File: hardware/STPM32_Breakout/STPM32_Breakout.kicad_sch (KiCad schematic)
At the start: 0 parts

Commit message: Complete compact STPM32 breakout
Implement the isolated 9 VAC and current-output CT front end, compact breadboard PCB, routed ground planes, validation scripts, and design documentation.

Co-authored-by: Copilot <223556219+Copilot@users.noreply.github.com>
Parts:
- added C1, C2: 330n, Capacitor_SMD:C_0603_1608Metric, symbol Device:C
- added C10, C9: 1u, Capacitor_SMD:C_0805_2012Metric, symbol Device:C
- added C11: 4.7u, Capacitor_SMD:C_0805_2012Metric, symbol Device:C
- added C12: 100n, Capacitor_SMD:C_0603_1608Metric, symbol Device:C
- added C13, C14: 15p, Capacitor_SMD:C_0603_1608Metric, symbol Device:C
- added C3, C4: 33n, Capacitor_SMD:C_0603_1608Metric, symbol Device:C
- added J1: BREADBOARD I/O, Connector_PinHeader_2.54mm:PinHeader_1x12_P2.54mm_Vertical, symbol Connector_Generic:Conn_01x12
- added NT1: ANALOG/DIGITAL STAR, NetTie:NetTie-3_SMD_Pad0.5mm, symbol Connector_Generic:Conn_01x03
- added R1, R2: 100R, Resistor_SMD:R_0603_1608Metric, symbol Device:R
- added R10, R9: 1k, Resistor_SMD:R_0603_1608Metric, symbol Device:R
- added R11, R12: 10k, Resistor_SMD:R_0603_1608Metric, symbol Device:R
- added R3, R4, R6, R7: 100k, Resistor_SMD:R_0603_1608Metric, symbol Device:R
- added R5, R8: 2.49k, Resistor_SMD:R_0603_1608Metric, symbol Device:R
- added RB1: 2.4R, Resistor_SMD:R_0603_1608Metric, symbol Device:R
- added SW1: RESET, Button_Switch_SMD:SW_SPST_CK_RS282G05A3, symbol Switch:SW_Push
- added TP1: INT1, TestPoint:TestPoint_Pad_D1.5mm, symbol Connector_Generic:Conn_01x01
- added TP2: LED1, TestPoint:TestPoint_Pad_D1.5mm, symbol Connector_Generic:Conn_01x01
- added TP3: LED2, TestPoint:TestPoint_Pad_D1.5mm, symbol Connector_Generic:Conn_01x01
- added TP4: CLKOUT_ZCR, TestPoint:TestPoint_Pad_D1.5mm, symbol Connector_Generic:Conn_01x01
- added U1: STPM32, Package_DFN_QFN:VQFN-24-1EP_4x4mm_P0.5mm_EP2.45x2.45mm, symbol STPM3x:STPM32
- added Y1: 16MHz, Crystal:Crystal_SMD_3225-4Pin_3.2x2.5mm, symbol Device:Crystal
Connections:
- new net +3V3: C9.1, J1.1 (Pin_1), R11.1, U1.17 (VCC)
- new net AGND: C1.2, C10.2, C2.2, C3.2, C4.2, NT1.1 (Pin_1), R5.2, R8.2, U1.14 (GNDA), U1.16 (GND_REG)
- new net CLKOUT_ZCR: TP4.1 (Pin_1), U1.1 (CLKOUT/ZCR)
- new net CT_N: J1.6 (Pin_6), R2.1, RB1.2
- new net CT_P: J1.5 (Pin_5), R1.1, RB1.1
- new net DGND: C11.2, C13.2, C14.2, C9.2, J1.2 (Pin_2), NT1.3 (Pin_3), R12.2, SW1.2, U1.18 (GNDD)
- new net EN: J1.12 (Pin_12), R11.2, SW1.1, U1.7 (EN)
- new net GND_REF: C12.2, NT1.2 (Pin_2), U1.13 (GND_REF)
- new net IIN1: C2.1, R2.2, U1.11 (IIN1)
- new net IIP1: C1.1, R1.2, U1.10 (IIP1)
- new net INT1: TP1.1 (Pin_1), U1.6 (INT1)
- new net LED1: TP2.1 (Pin_1), U1.4 (LED1)
- new net LED2: TP3.1 (Pin_1), U1.5 (LED2)
- new net MISO_TXD: J1.10 (Pin_10), U1.24 (MISO/TXD)
- new net MOSI_RXD: J1.9 (Pin_9), U1.23 (MOSI/RXD)
- new net SCL: J1.8 (Pin_8), U1.22 (SCL)
- new net SCS: J1.7 (Pin_7), R12.1, U1.21 (SCS)
- new net SYN: J1.11 (Pin_11), U1.20 (SYN)
- new net VAC_N: J1.4 (Pin_4), R6.1
- new net VAC_N_MID: R6.2, R7.1
- new net VAC_P: J1.3 (Pin_3), R3.1
- new net VAC_P_MID: R3.2, R4.1
- new net VDDA: C10.1, U1.15 (VDDA)
- new net VDDD: C11.1, U1.19 (VDDD)
- new net VDIV_N: R10.1, R7.2, R8.1
- new net VDIV_P: R4.2, R5.1, R9.1
- new net VIN1: C4.1, R10.2, U1.9 (VIN1)
- new net VIP1: C3.1, R9.2, U1.8 (VIP1)
- new net VREF1: C12.1, U1.12 (VREF1)
- new net XTAL1: C13.1, U1.3 (XTAL1), Y1.1
- new net XTAL2: C14.1, U1.2 (CLKIN/XTAL2), Y1.2
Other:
- note added: "CURRENT HEADER INPUT: 100 A : 50 mA current-output CT 2.4 ohm burden = 120 mV RMS at 100 A; approximately 4.8 kHz LPF."
- note added: "SCS is pulled low for SPI default; drive high before reset to select UART."
- note added: "VOLTAGE HEADER INPUT: isolated 9 VAC transformer secondary only 200k/2.49k symmetric divider = approx. 111 mV RMS differential at 9 VAC."
- note added: "WARNING: NOT A CERTIFIED ISOLATION BARRIER. Never connect J1 directly to mains."
- title: STPM32 Breakout -> STPM32 Energy Metering Breakout

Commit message: Add Elecrow BOM for STPM32
Co-authored-by: Copilot <223556219+Copilot@users.noreply.github.com>
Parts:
- C1, C2: Assembly (none) -> SMT; LCSC (none) -> C282682; MPN (none) -> TCC0603X7R334K500CT; Manufacturer (none) -> CCTC; Package (none) -> 0603 (1608 Metric); Purchase URL (none) -> https://www.lcsc.com/product-detail/C282682.html
- C10, C9: Assembly (none) -> SMT; LCSC (none) -> C116352; MPN (none) -> CL21B105KAFNNNE; Manufacturer (none) -> Samsung Electro-Mechanics; Package (none) -> 0805 (2012 Metric); Purchase URL (none) -> https://www.lcsc.com/product-detail/C116352.html
- C11: Assembly (none) -> SMT; LCSC (none) -> C16194928; MPN (none) -> CL21A475KOFNNNG; Manufacturer (none) -> Samsung Electro-Mechanics; Package (none) -> 0805 (2012 Metric); Purchase URL (none) -> https://www.lcsc.com/product-detail/C16194928.html
- C12: Assembly (none) -> SMT; LCSC (none) -> C1591; MPN (none) -> CL10B104KB8NNNC; Manufacturer (none) -> Samsung Electro-Mechanics; Package (none) -> 0603 (1608 Metric); Purchase URL (none) -> https://www.lcsc.com/product-detail/C1591.html
- C13, C14: Assembly (none) -> SMT; LCSC (none) -> C1644; MPN (none) -> CL10C150JB8NNNC; Manufacturer (none) -> Samsung Electro-Mechanics; Package (none) -> 0603 (1608 Metric); Purchase URL (none) -> https://www.lcsc.com/product-detail/C1644.html
- C3, C4: Assembly (none) -> SMT; LCSC (none) -> C21117; MPN (none) -> CL10B333KB8NNNC; Manufacturer (none) -> Samsung Electro-Mechanics; Package (none) -> 0603 (1608 Metric); Purchase URL (none) -> https://www.lcsc.com/product-detail/C21117.html
- J1: Assembly (none) -> THT; LCSC (none) -> C2840012; MPN (none) -> PZ254V-11-12P; Manufacturer (none) -> XFCN; Notes (none) -> Quote THT assembly separately and confirm pin protrusion su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; Package (none) -> 1x12, 2.54 mm pitch, vertical THT; Purchase URL (none) -> https://www.lcsc.com/product-detail/C2840012.html
- NT1, TP1, TP2, TP3, TP4: now left out of the parts list
- R1, R2: Assembly (none) -> SMT; LCSC (none) -> C105588; MPN (none) -> RC0603FR-07100RL; Manufacturer (none) -> YAGEO; Package (none) -> 0603 (1608 Metric); Purchase URL (none) -> https://www.lcsc.com/product-detail/C105588.html
- R10, R9: Assembly (none) -> SMT; LCSC (none) -> C22548; MPN (none) -> RC0603FR-071KL; Manufacturer (none) -> YAGEO; Package (none) -> 0603 (1608 Metric); Purchase URL (none) -> https://www.lcsc.com/product-detail/C22548.html
- R11, R12: Assembly (none) -> SMT; LCSC (none) -> C98220; MPN (none) -> RC0603FR-0710KL; Manufacturer (none) -> YAGEO; Package (none) -> 0603 (1608 Metric); Purchase URL (none) -> https://www.lcsc.com/product-detail/C98220.html
- R3, R4, R6, R7: Assembly (none) -> SMT; LCSC (none) -> C122538; MPN (none) -> RT0603BRD07100KL; Manufacturer (none) -> YAGEO; Notes (none) -> Use one lot for all four voltage-divider resistors.; Package (none) -> 0603 (1608 Metric); Purchase URL (none) -> https://www.lcsc.com/product-detail/C122538.html
- R5, R8: Assembly (none) -> SMT; LCSC (none) -> C861299; MPN (none) -> RT0603BRD072K49L; Manufacturer (none) -> YAGEO; Notes (none) -> Use one lot for the matched voltage-divider low sides.; Package (none) -> 0603 (1608 Metric); Purchase URL (none) -> https://www.lcsc.com/product-detail/C861299.html
- RB1: Assembly (none) -> SMT; LCSC (none) -> C137746; MPN (none) -> RC0603FR-072R4L; Manufacturer (none) -> YAGEO; Notes (none) -> About 6 mW at 50 mA RMS. The 200 ppm/C TCR is suitable for 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; Package (none) -> 0603 (1608 Metric); Purchase URL (none) -> https://www.lcsc.com/product-detail/C137746.html
- SW1: Assembly (none) -> SMT; LCSC (none) -> C221930; MPN (none) -> RS-282G05A3-SMRT; Manufacturer (none) -> C&K; Package (none) -> C&K RS-282G05A3 SMD; Purchase URL (none) -> https://www.lcsc.com/product-detail/C221930.html
- U1: Assembly (none) -> SMT; LCSC (none) -> C128380; MPN (none) -> STPM32TR; Manufacturer (none) -> STMicroelectronics; Notes (none) -> Inspect exposed-pad paste and voiding during DFM review.; Package (none) -> VQFN-24-EP, 4 x 4 mm, 0.5 mm pitch; Purchase URL (none) -> https://www.lcsc.com/product-detail/C128380.html
- Y1: Assembly (none) -> SMT; LCSC (none) -> C12668; MPN (none) -> X322516MOB4SI; Manufacturer (none) -> YXC; Notes (none) -> 12 pF load is consistent with two 15 pF capacitors plus est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; Package (none) -> SMD3225-4P; Purchase URL (none) -> https://www.lcsc.com/product-detail/C12668.html

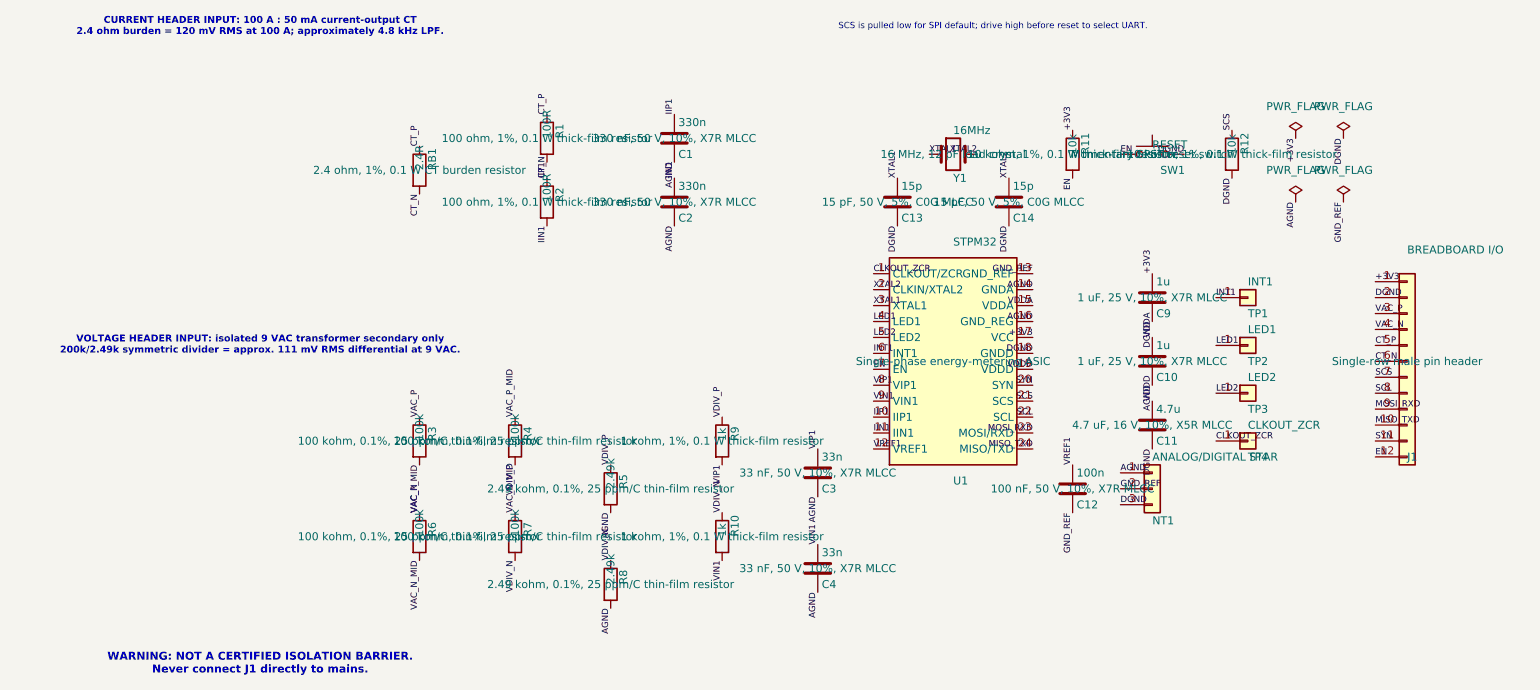
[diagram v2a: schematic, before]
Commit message: Add STPM32 SPI UART mode selector
Co-authored-by: Copilot <223556219+Copilot@users.noreply.github.com>
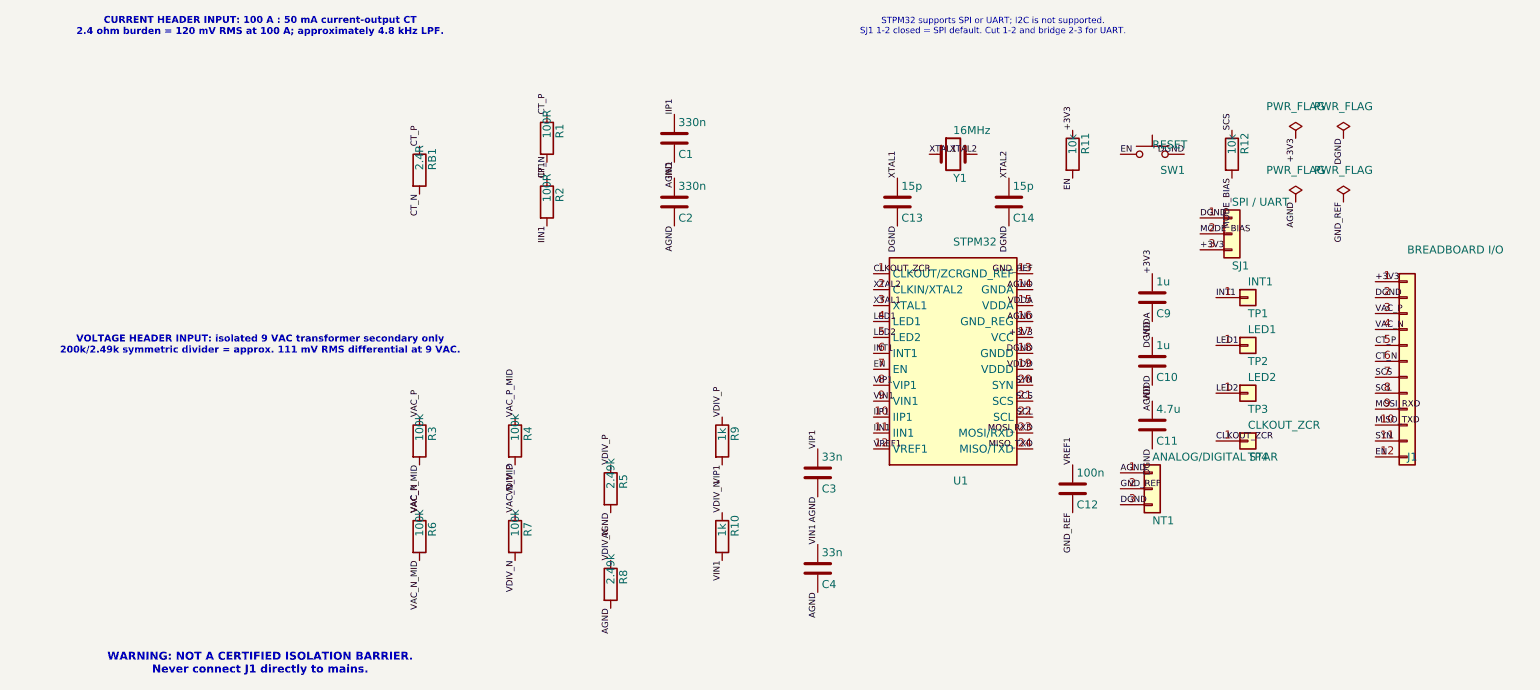
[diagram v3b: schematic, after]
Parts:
- added SJ1: SPI / UART, Jumper:SolderJumper-3_P1.3mm_Bridged12_Pad1.0x1.5mm, symbol Connector_Generic:Conn_01x03
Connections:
- net +3V3: now also SJ1.3 (Pin_3)
- net DGND: now also SJ1.1 (Pin_1); no longer R12.2
- new net MODE_BIAS: R12.2, SJ1.2 (Pin_2)
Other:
- note added: "STPM32 supports SPI or UART; I2C is not supported. SJ1 1-2 closed = SPI default. Cut 1-2 and bridge 2-3 for UART."
- note removed: "SCS is pulled low for SPI default; drive high before reset to select UART."
